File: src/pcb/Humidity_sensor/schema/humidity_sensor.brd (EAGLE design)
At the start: 23.8 x 25.4 mm, 6 parts, among them U1 SL876Q5A001T001000

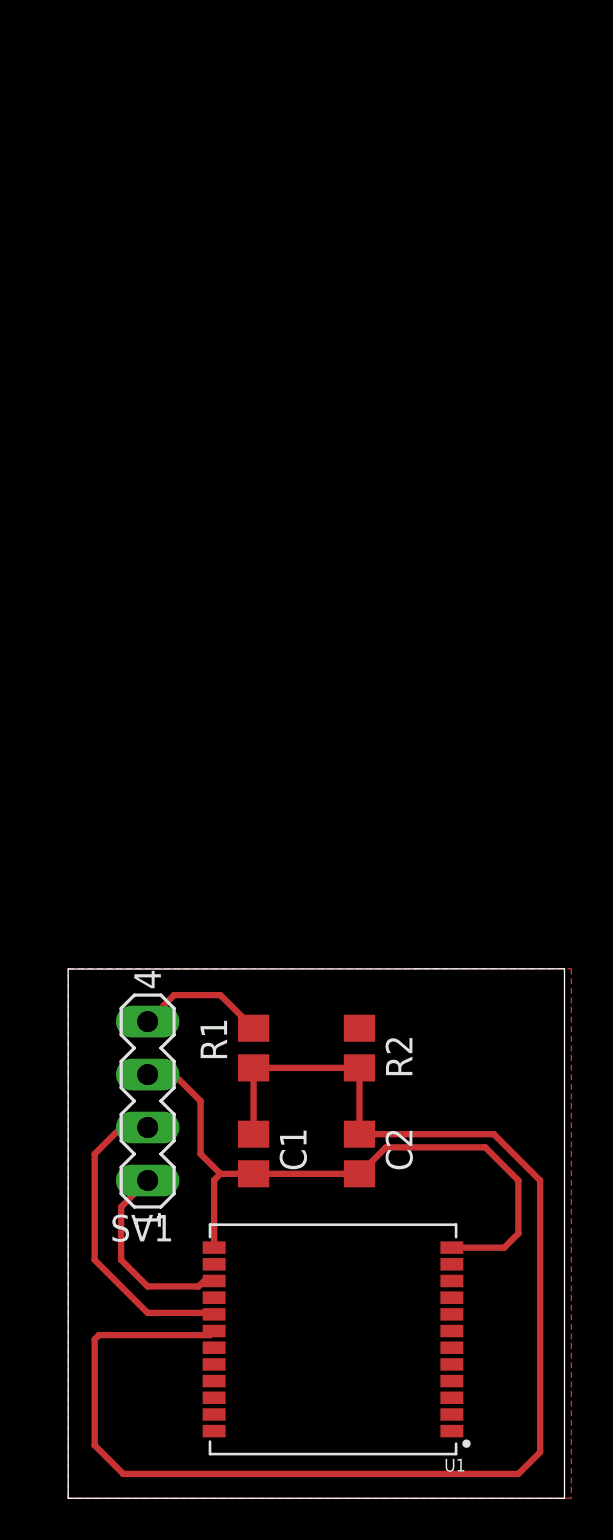
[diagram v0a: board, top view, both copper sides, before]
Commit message: added humidity sensor scheme, board scheme, images and updated GPS module
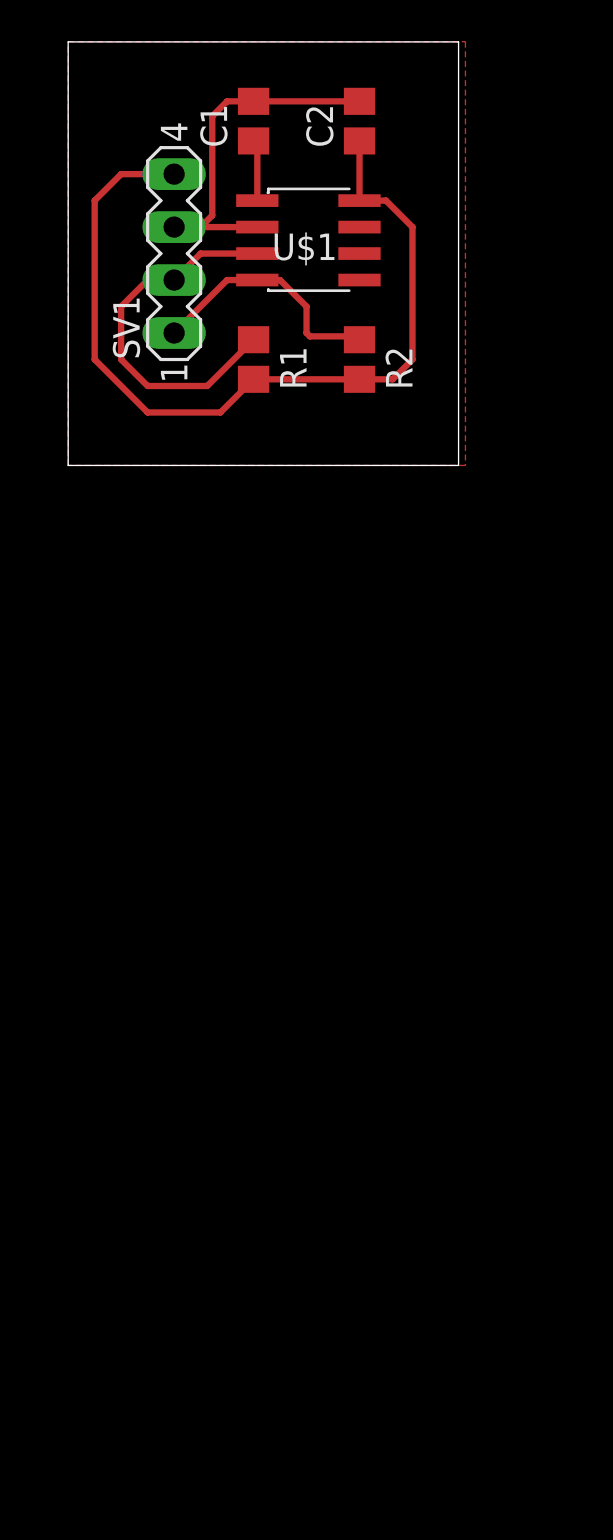
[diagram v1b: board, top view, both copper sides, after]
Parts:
- removed U1: SL876Q5A001T001000, SL876Q5A001T001000:XCVR_SL876Q5A001T001000
- added U$1: (no value), HIH6030-021-001:HIH6030-021-001
- C1: value 10µF -> 0.1µF
- C2: value 100nF -> 0.22µF
- R1: value 100 -> 2.2k
- R2: value 120 -> 2.2k
- moved C1 49.5 mm to (8.89, 76.2), turned to 90 degrees
- moved C2 49.5 mm to (14.0, 76.2), turned to 90 degrees
- moved SV1 40.7 mm to (5.08, 69.8)
- moved R1 33.0 mm to (8.89, 64.8), turned to 270 degrees
- moved R2 33.0 mm to (14.0, 64.8)
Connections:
- removed net RX: SV1.1, U1.15
- removed net TX: SV1.2, U1.17
- removed net VIN: C1.1, C2.1, R1.1, R2.2, U1.18
- new net SCL: R1.1, SV1.2, U$1.3
- new net SDA: R2.1, SV1.1, U$1.4
- new net VCORE: C1.1, U$1.1
- net GND: now also U$1.2; no longer R2.1, U1.10, U1.12, U1.13, U1.2, U1.20, U1.24, U1.3, U1.5
- net VDD: now also C2.1, R2.2, U$1.8
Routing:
- net VIN: track 67.4 -> 0.00 mm
- net VDD: track 6.26 -> 42.0 mm
- net SCL: track 0.00 -> 18.4 mm
- net GND: track 32.1 -> 17.0 mm
- net TX: track 15.0 -> 0.00 mm
- net SDA: track 0.00 -> 12.4 mm
- net RX: track 9.43 -> 0.00 mm
- net VCORE: track 0.00 -> 2.93 mm
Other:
- board size 23.8 x 25.4 mm -> 18.7 x 20.3 mm

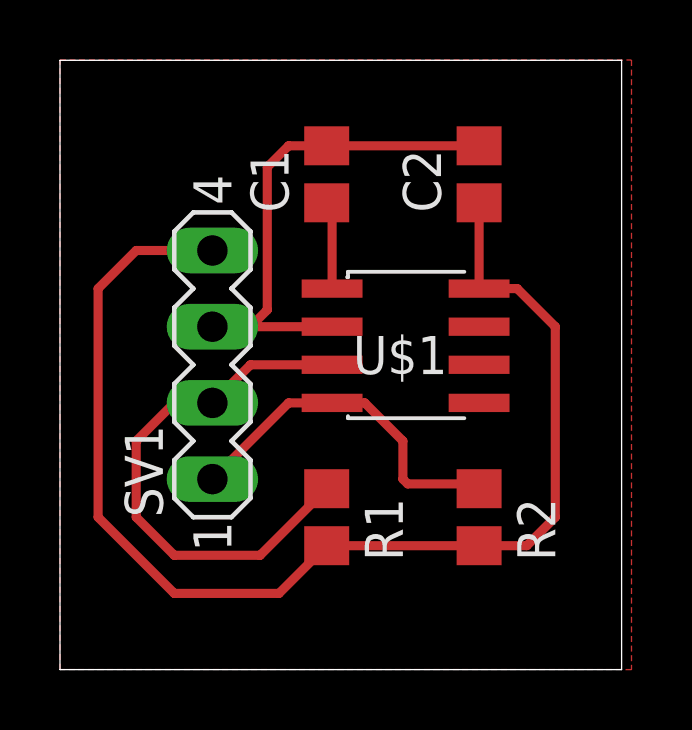
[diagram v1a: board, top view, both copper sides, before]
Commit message: updated footprint, humidity sensor pcb, gps module pcb and images, added gerberfiles
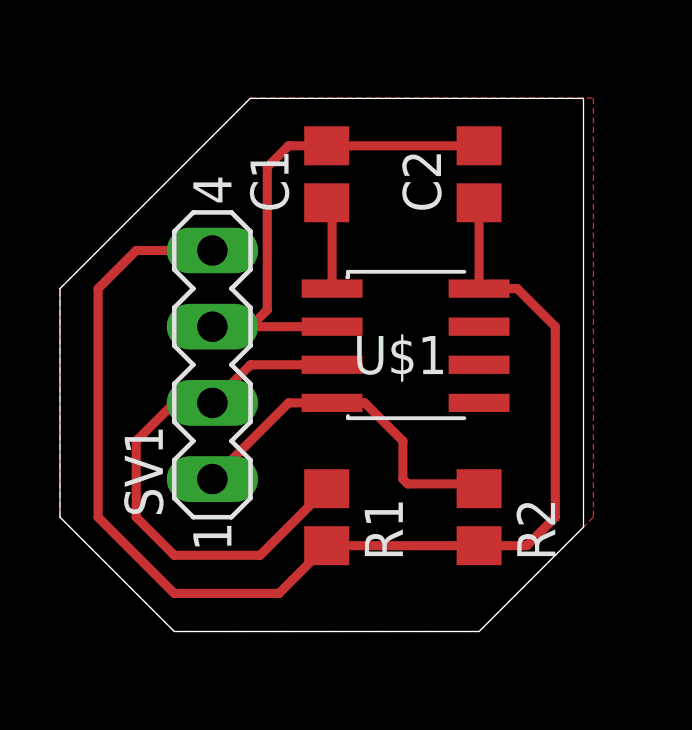
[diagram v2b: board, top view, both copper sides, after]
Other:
- board size 18.7 x 20.3 mm -> 17.4 x 17.8 mm
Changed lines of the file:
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@@
 <drawing>
 <settings>
-<setting alwaysvectorfont="no"/>
+<setting alwaysvectorfont="yes"/>
 <setting verticaltext="up"/>
 </settings>
@@
 </layers>
 <board>
+<fusionsync huburn="a.YnVzaW5lc3M6aG90bWFpbDY1Mzg5" projecturn="a.YnVzaW5lc3M6aG90bWFpbDY1Mzg5I0QyMDE5MDkyODIyMDA1ODM3Ng" f3durn="urn:adsk.wipprod:dm.lineage:svLPsV9RS2u_rmbosFshIg" pcbguid="6507b553-2b27-457c-9f5c-4fa8c74f7b8c" lastpulledtime="" lastsyncedchangeguid="78f34180-aae0-3ad1-317f-4908479c897f"/>
 <plain>
-<wire x1="0" y1="59.69" x2="18.72" y2="59.69" width="0" layer="20"/>
-<wire x1="18.72" y1="59.69" x2="18.72" y2="80" width="0" layer="20"/>
-<wire x1="18.72" y1="80" x2="0" y2="80" width="0" layer="20"/>
-<wire x1="0" y1="80" x2="0" y2="59.69" width="0" layer="20"/>
-<dimension x1="0" y1="80" x2="0" y2="59.69" x3="-1.27" y3="69.845" textsize="1.778" layer="1"/>
-<dimension x1="0" y1="80" x2="18.72" y2="80" x3="9.36" y3="81.28" textsize="1.778" layer="1"/>
+<wire x1="17.45" y1="64.44" x2="17.45" y2="78.73" width="0" layer="20"/>
+<wire x1="17.45" y1="78.73" x2="6.34" y2="78.73" width="0" layer="20"/>
+<wire x1="6.34" y1="78.73" x2="0" y2="72.39" width="0" layer="20"/>
+<wire x1="0" y1="72.39" x2="0" y2="64.77" width="0" layer="20"/>
+<wire x1="0" y1="64.77" x2="3.809996875" y2="60.960003125" width="0" layer="20"/>
+<wire x1="3.809996875" y1="60.960003125" x2="13.970003125" y2="60.960003125" width="0" layer="20"/>
+<wire x1="13.970003125" y1="60.960003125" x2="17.45" y2="64.44" width="0" layer="20"/>
 </plain>
 <attributes>
@@
 </class>
 </classes>
-<designrules name="default">
+<designrules name="default *">
 <description language="de">&lt;b&gt;EAGLE Design Rules&lt;/b&gt;
 &lt;p&gt;
@@
 <param name="mdViaViaSameLayer" value="6mil"/>
 <param name="mnLayersViaInSmd" value="2"/>
-<param name="mdCopperDimension" value="40mil"/>
+<param name="mdCopperDimension" value="0mil"/>
 <param name="mdDrill" value="6mil"/>
 <param name="mdSmdStop" value="0mil"/>
@@
 <wire x1="9.07" y1="71.12" x2="6.35" y2="71.12" width="0.3048" layer="1"/>
 <polygon width="0.1524" layer="1">
-<vertex x="0" y="80.01"/>
-<vertex x="19.05" y="80.01"/>
-<vertex x="19.05" y="59.69"/>
-<vertex x="0" y="59.69"/>
+<vertex x="0" y="72.39"/>
+<vertex x="6.35" y="78.74"/>
+<vertex x="17.78" y="78.74"/>
+<vertex x="17.78" y="64.77"/>
+<vertex x="13.97" y="60.96"/>
+<vertex x="3.81" y="60.96"/>
+<vertex x="0" y="64.77"/>
 </polygon>
 </signal>
@@
 </note>
 <note version="8.3" severity="warning">
+Since Version 8.3, EAGLE supports Fusion synchronisation.
+This feature will not be available in this version and saving
+the document will break the link to the Fusion PCB feature.
+</note>
+<note version="8.3" severity="warning">

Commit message: Merge conflict fix
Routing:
- net VDD: track 42.0 -> 41.3 mm
- net SCL: track 18.4 -> 17.6 mm
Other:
- board size 17.4 x 17.8 mm -> 21.3 x 20.3 mm
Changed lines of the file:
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@@
 <layer number="43" name="vRestrict" color="2" fill="10" visible="yes" active="yes"/>
 <layer number="44" name="Drills" color="7" fill="1" visible="no" active="yes"/>
-<layer number="45" name="Holes" color="7" fill="1" visible="no" active="yes"/>
+<layer number="45" name="Holes" color="7" fill="1" visible="yes" active="yes"/>
 <layer number="46" name="Milling" color="3" fill="1" visible="no" active="yes"/>
 <layer number="47" name="Measures" color="7" fill="1" visible="no" active="yes"/>
@@
 <fusionsync huburn="a.YnVzaW5lc3M6c3R1ZGVudDk3MjU" projecturn="a.YnVzaW5lc3M6c3R1ZGVudDk3MjUjRDIwMTkxMDA0MjIyNzk2ODA2" f3durn="urn:adsk.wipprod:dm.lineage:UIVqwKJnQp60m9CcjEivng" pcbguid="37e22aa0-a2bb-4ea8-995d-bf2bfafcd302" lastpulledtime="" lastsyncedchangeguid="5d00073d-4eff-7592-cb1e-6a147588d151"/>
 <plain>
-<wire x1="17.45" y1="64.44" x2="17.45" y2="78.73" width="0" layer="20"/>
-<wire x1="17.45" y1="78.73" x2="6.34" y2="78.73" width="0" layer="20"/>
-<wire x1="6.34" y1="78.73" x2="0" y2="72.39" width="0" layer="20"/>
-<wire x1="0" y1="72.39" x2="0" y2="64.77" width="0" layer="20"/>
-<wire x1="0" y1="64.77" x2="3.809996875" y2="60.960003125" width="0" layer="20"/>
-<wire x1="3.809996875" y1="60.960003125" x2="13.970003125" y2="60.960003125" width="0" layer="20"/>
-<wire x1="13.970003125" y1="60.960003125" x2="17.45" y2="64.44" width="0" layer="20"/>
+<wire x1="-1.27" y1="80" x2="-1.27" y2="59.690003125" width="0" layer="20"/>
+<wire x1="-1.27" y1="59.690003125" x2="19.99" y2="59.690003125" width="0" layer="20"/>
+<wire x1="19.99" y1="59.690003125" x2="19.99" y2="80" width="0" layer="20"/>
+<wire x1="19.99" y1="80" x2="-1.27" y2="80" width="0" layer="20"/>
+<hole x="1.27" y="77.47" drill="3"/>
+<hole x="17.78" y="62.23" drill="3"/>
+<hole x="17.78" y="77.47" drill="3"/>
+<hole x="1.27" y="62.23" drill="3"/>
 </plain>
 <attributes>
@@
 <wire x1="2.54" y1="73.66" x2="1.27" y2="72.39" width="0.3048" layer="1"/>
 <wire x1="13.97" y1="75.25" x2="13.97" y2="72.39" width="0.3048" layer="1"/>
-<wire x1="1.27" y1="72.39" x2="1.27" y2="64.77" width="0.3048" layer="1"/>
-<wire x1="1.27" y1="64.77" x2="3.81" y2="62.23" width="0.3048" layer="1"/>
-<wire x1="3.81" y1="62.23" x2="7.3" y2="62.23" width="0.3048" layer="1"/>
+<wire x1="1.27" y1="72.39" x2="1.27" y2="66.04" width="0.3048" layer="1"/>
+<wire x1="1.27" y1="66.04" x2="5.08" y2="62.23" width="0.3048" layer="1"/>
+<wire x1="5.08" y1="62.23" x2="7.3" y2="62.23" width="0.3048" layer="1"/>
 <wire x1="7.3" y1="62.23" x2="8.89" y2="63.82" width="0.3048" layer="1"/>
 </signal>
@@
 <wire x1="8.89" y1="65.72" x2="9.21" y2="66.04" width="0.3048" layer="1"/>
 <wire x1="8.89" y1="65.72" x2="6.67" y2="63.5" width="0.3048" layer="1"/>
-<wire x1="3.81" y1="63.5" x2="2.54" y2="64.77" width="0.3048" layer="1"/>
-<wire x1="2.54" y1="64.77" x2="2.54" y2="67.31" width="0.3048" layer="1"/>
+<wire x1="5.08" y1="63.5" x2="2.54" y2="66.04" width="0.3048" layer="1"/>
+<wire x1="2.54" y1="66.04" x2="2.54" y2="67.31" width="0.3048" layer="1"/>
 <wire x1="2.54" y1="67.31" x2="3.81" y2="68.58" width="0.3048" layer="1"/>
 <wire x1="3.81" y1="68.58" x2="5.08" y2="68.58" width="0.3048" layer="1"/>
-<wire x1="6.67" y1="63.5" x2="3.81" y2="63.5" width="0.3048" layer="1"/>
+<wire x1="6.67" y1="63.5" x2="5.08" y2="63.5" width="0.3048" layer="1"/>
 </signal>
 <signal name="SDA">
@@
 <wire x1="9.07" y1="71.12" x2="6.35" y2="71.12" width="0.3048" layer="1"/>
 <polygon width="0.1524" layer="1">
-<vertex x="0" y="72.39"/>
-<vertex x="6.35" y="78.74"/>
-<vertex x="17.78" y="78.74"/>
-<vertex x="17.78" y="64.77"/>
-<vertex x="13.97" y="60.96"/>
-<vertex x="3.81" y="60.96"/>
-<vertex x="0" y="64.77"/>
+<vertex x="-1.27" y="59.69"/>
+<vertex x="-1.27" y="80.01"/>
+<vertex x="20.32" y="80.01"/>
+<vertex x="20.32" y="59.69"/>
 </polygon>
 </signal>
